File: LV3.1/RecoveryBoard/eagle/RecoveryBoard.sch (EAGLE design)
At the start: 90 parts, among them IC1 BD62120AEFJ-E2, Q6 MOSFET-PCH-SOT23-6, U1 STM32F042K6, U10 TPS63070, Y1 ECS-160-10-36Q-ES-TR

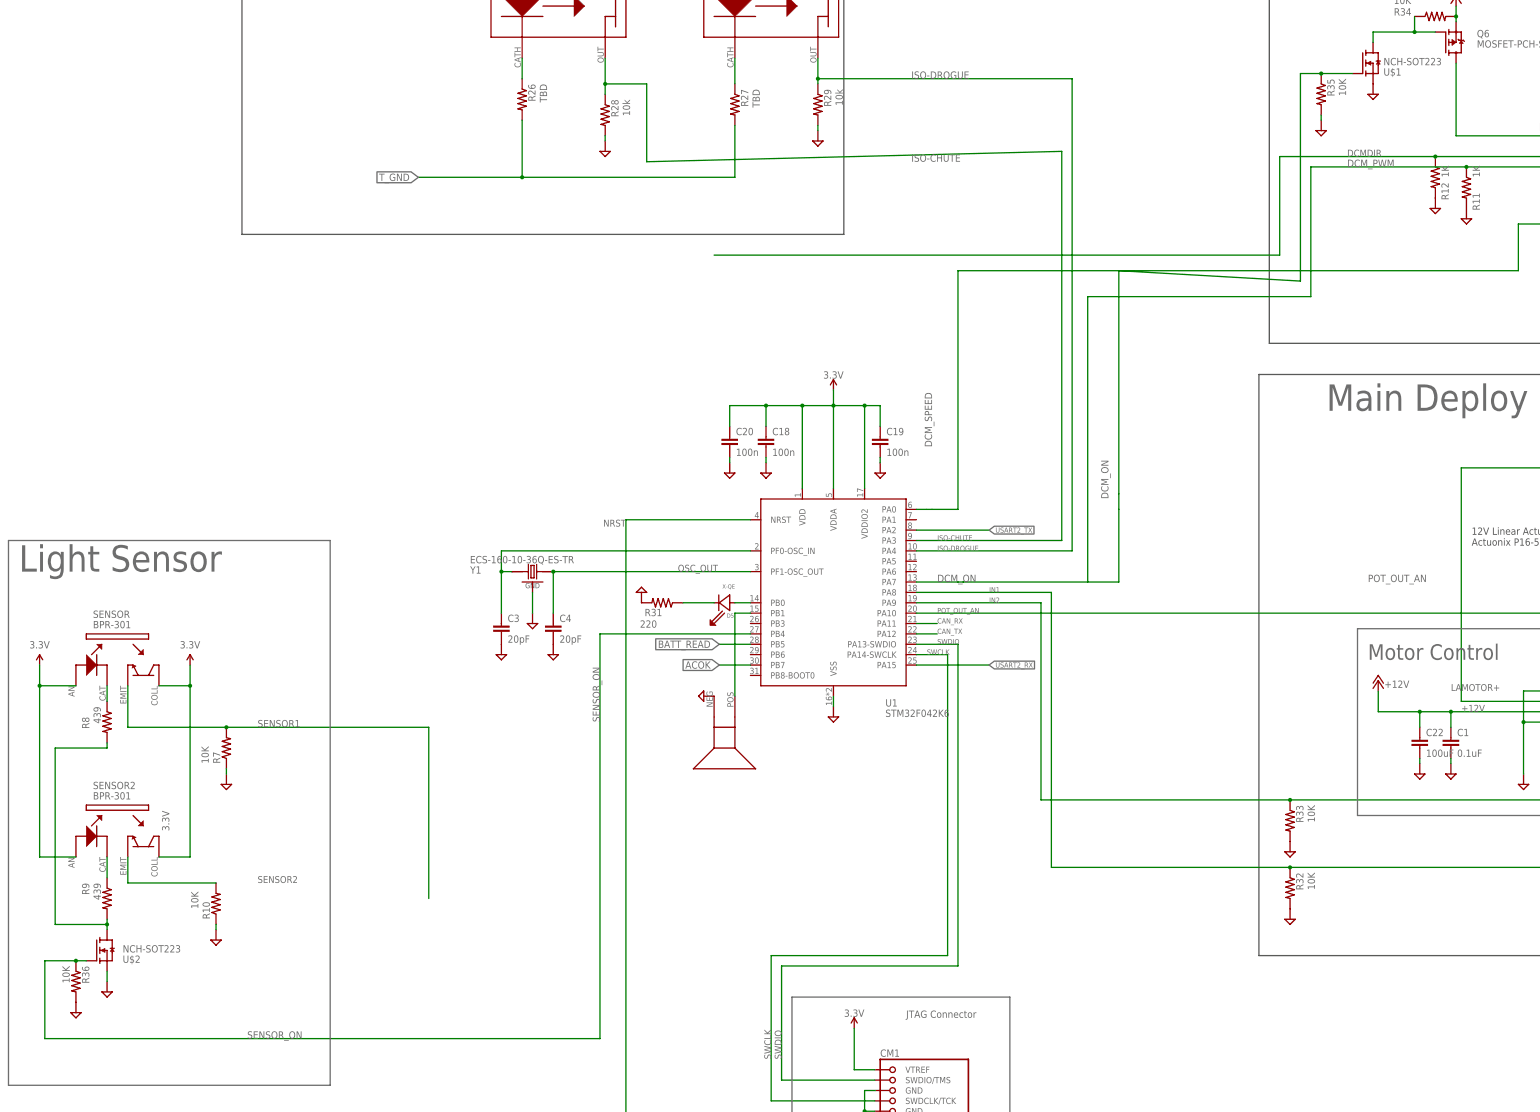
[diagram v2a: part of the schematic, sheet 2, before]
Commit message: beginning routing and placement
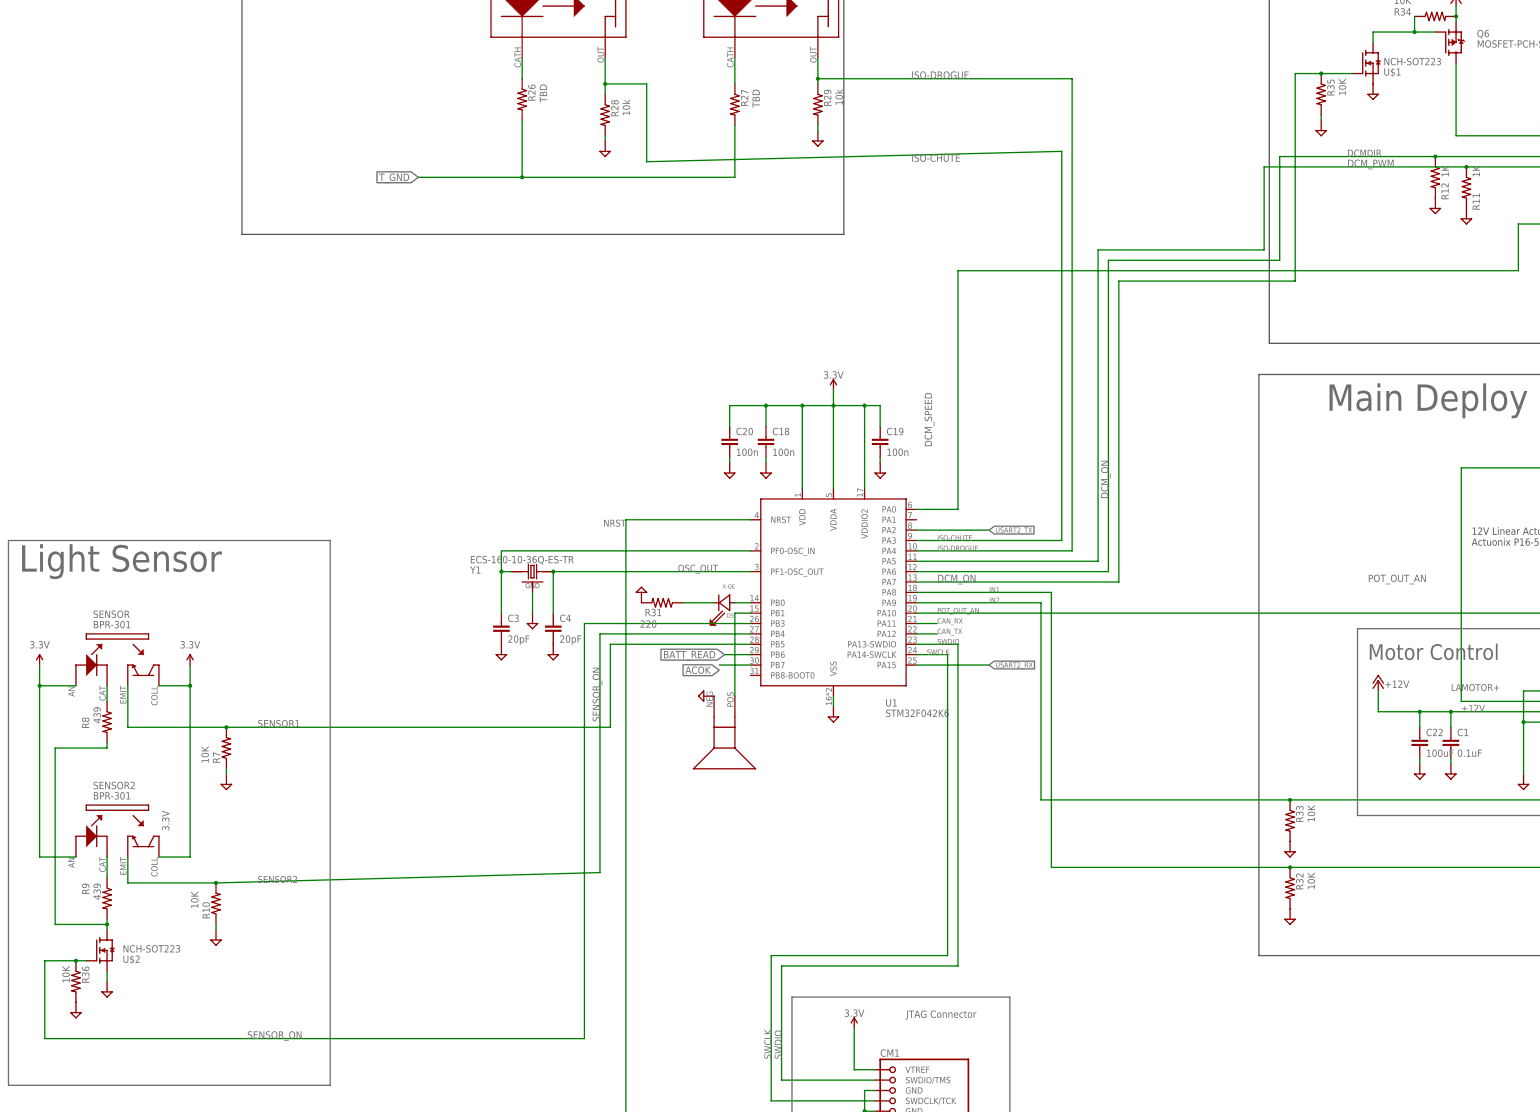
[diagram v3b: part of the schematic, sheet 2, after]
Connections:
- net BATT_READ: now also U1.PB6; no longer U1.PB5
- net DCMDIR: now also U1.PA6
- net DCM_PWM: now also U1.PA5
- net SENSOR1: now also U1.PB5
- net SENSOR2: now also U1.PB4
- net SENSOR_ON: now also U1.PB3; no longer U1.PB4
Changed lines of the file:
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@@
 <net name="SENSOR1" class="0">
 <segment>
-<wire x1="125.73" y1="152.4" x2="175.26" y2="152.4" width="0.1524" layer="91"/>
-<wire x1="175.26" y1="152.4" x2="175.26" y2="110.49" width="0.1524" layer="91"/>
+<wire x1="125.73" y1="152.4" x2="219.71" y2="152.4" width="0.1524" layer="91"/>
 <pinref part="R7" gate="R" pin="2"/>
 <pinref part="SENSOR" gate="BPR-301" pin="EMIT"/>
@@
 <junction x="125.73" y="152.4"/>
 <label x="133.35" y="152.4" size="1.778" layer="95"/>
+<pinref part="U1" gate="G$1" pin="PB5"/>
+<wire x1="219.71" y1="172.72" x2="219.71" y2="152.4" width="0.1524" layer="91"/>
+<wire x1="219.71" y1="172.72" x2="254" y2="172.72" width="0.1524" layer="91"/>
 </segment>
 </net>
@@
 <segment>
 <label x="400.05" y="292.1" size="1.6764" layer="95"/>
-<wire x1="245.11" y1="267.97" x2="383.54" y2="267.97" width="0.1524" layer="91"/>
-<wire x1="383.54" y1="267.97" x2="383.54" y2="292.1" width="0.1524" layer="91"/>
+<wire x1="341.63" y1="266.7" x2="383.54" y2="266.7" width="0.1524" layer="91"/>
+<wire x1="383.54" y1="266.7" x2="383.54" y2="292.1" width="0.1524" layer="91"/>
 <pinref part="J1" gate="A" pin="3"/>
 <wire x1="468.63" y1="292.1" x2="421.64" y2="292.1" width="0.1524" layer="91"/>
@@
 <pinref part="R12" gate="R" pin="1"/>
 <junction x="421.64" y="292.1"/>
+<wire x1="341.63" y1="190.5" x2="341.63" y2="266.7" width="0.1524" layer="91"/>
+<pinref part="U1" gate="G$1" pin="PA6"/>
+<wire x1="294.64" y1="190.5" x2="341.63" y2="190.5" width="0.1524" layer="91"/>
 </segment>
 </net>
 <net name="SENSOR_ON" class="0">
 <segment>
-<wire x1="217.17" y1="175.26" x2="217.17" y2="76.2" width="0.1524" layer="91"/>
-<wire x1="217.17" y1="76.2" x2="81.28" y2="76.2" width="0.1524" layer="91"/>
+<wire x1="213.36" y1="177.8" x2="213.36" y2="76.2" width="0.1524" layer="91"/>
+<wire x1="213.36" y1="76.2" x2="81.28" y2="76.2" width="0.1524" layer="91"/>
 <wire x1="81.28" y1="76.2" x2="81.28" y2="95.25" width="0.1524" layer="91"/>
 <wire x1="81.28" y1="95.25" x2="88.9" y2="95.25" width="0.1524" layer="91"/>
@@
 <wire x1="88.9" y1="95.25" x2="91.44" y2="95.25" width="0.1524" layer="91"/>
 <junction x="88.9" y="95.25"/>
-<pinref part="U1" gate="G$1" pin="PB4"/>
-<wire x1="254" y1="175.26" x2="217.17" y2="175.26" width="0.1524" layer="91"/>
 <label x="217.17" y="153.67" size="1.778" layer="95" rot="R90"/>
 <label x="130.81" y="76.2" size="1.778" layer="95"/>
+<pinref part="U1" gate="G$1" pin="PB3"/>
+<wire x1="213.36" y1="177.8" x2="254" y2="177.8" width="0.1524" layer="91"/>
 </segment>
 </net>
@@
 <wire x1="101.6" y1="114.3" x2="101.6" y2="120.65" width="0.1524" layer="91"/>
 <label x="133.35" y="114.3" size="1.6764" layer="95"/>
+<wire x1="123.19" y1="114.3" x2="217.17" y2="116.84" width="0.1524" layer="91"/>
+<wire x1="217.17" y1="116.84" x2="217.17" y2="175.26" width="0.1524" layer="91"/>
+<junction x="123.19" y="114.3"/>
+<pinref part="U1" gate="G$1" pin="PB4"/>
+<wire x1="254" y1="175.26" x2="217.17" y2="175.26" width="0.1524" layer="91"/>
 </segment>
 </net>
@@
 <pinref part="J1" gate="A" pin="4"/>
 <wire x1="468.63" y1="289.56" x2="429.26" y2="289.56" width="0.1524" layer="91"/>
-<wire x1="429.26" y1="289.56" x2="391.16" y2="289.56" width="0.1524" layer="91"/>
+<wire x1="429.26" y1="289.56" x2="379.73" y2="289.56" width="0.1524" layer="91"/>
 <label x="400.05" y="289.56" size="1.778" layer="95"/>
 <pinref part="R11" gate="R" pin="1"/>
 <junction x="429.26" y="289.56"/>
-<wire x1="391.16" y1="257.81" x2="391.16" y2="289.56" width="0.1524" layer="91"/>
-<wire x1="391.16" y1="257.81" x2="336.55" y2="257.81" width="0.1524" layer="91"/>
-<wire x1="336.55" y1="257.81" x2="336.55" y2="187.96" width="0.1524" layer="91"/>
+<wire x1="379.73" y1="269.24" x2="379.73" y2="289.56" width="0.1524" layer="91"/>
+<wire x1="379.73" y1="269.24" x2="339.09" y2="269.24" width="0.1524" layer="91"/>
+<pinref part="U1" gate="G$1" pin="PA5"/>
+<wire x1="339.09" y1="193.04" x2="339.09" y2="269.24" width="0.1524" layer="91"/>
+<wire x1="339.09" y1="193.04" x2="294.64" y2="193.04" width="0.1524" layer="91"/>
 </segment>
 </net>
@@
 <pinref part="R35" gate="R" pin="1"/>
 <wire x1="401.32" y1="312.42" x2="393.7" y2="312.42" width="0.1524" layer="91"/>
-<wire x1="393.7" y1="312.42" x2="388.62" y2="312.42" width="0.1524" layer="91"/>
-<wire x1="388.62" y1="312.42" x2="388.62" y2="261.62" width="0.1524" layer="91"/>
-<wire x1="388.62" y1="261.62" x2="344.17" y2="264.16" width="0.1524" layer="91"/>
+<wire x1="393.7" y1="312.42" x2="387.35" y2="312.42" width="0.1524" layer="91"/>
+<wire x1="387.35" y1="312.42" x2="387.35" y2="261.62" width="0.1524" layer="91"/>
+<wire x1="387.35" y1="261.62" x2="344.17" y2="261.62" width="0.1524" layer="91"/>
 <junction x="393.7" y="312.42"/>
 <label x="341.63" y="208.28" size="1.778" layer="95" rot="R90"/>
-<wire x1="344.17" y1="264.16" x2="344.17" y2="209.55" width="0.1524" layer="91"/>
+<wire x1="344.17" y1="261.62" x2="344.17" y2="187.96" width="0.1524" layer="91"/>
 <pinref part="U1" gate="G$1" pin="PA7"/>
-<wire x1="344.17" y1="209.55" x2="344.17" y2="205.74" width="0.1524" layer="91"/>
-<wire x1="306.07" y1="187.96" x2="304.8" y2="187.96" width="0.1524" layer="91"/>
 <label x="299.72" y="187.96" size="1.778" layer="95"/>
-<wire x1="304.8" y1="187.96" x2="294.64" y2="187.96" width="0.1524" layer="91"/>
-<wire x1="306.07" y1="187.96" x2="344.17" y2="187.96" width="0.1524" layer="91"/>
-<wire x1="344.17" y1="187.96" x2="344.17" y2="205.74" width="0.1524" layer="91"/>
+<wire x1="294.64" y1="187.96" x2="344.17" y2="187.96" width="0.1524" layer="91"/>
 </segment>
 </net>
@@
 </segment>
 </net>
-<net name="BATT_READ" class="0">
-<segment>
-<pinref part="U1" gate="G$1" pin="PB5"/>
-<wire x1="254" y1="172.72" x2="246.38" y2="172.72" width="0.1524" layer="91"/>
-<label x="246.38" y="172.72" size="1.778" layer="95" rot="R180" xref="yes"/>
-</segment>
-</net>
 <net name="CAN_RX" class="0">
 <segment>
@@
 <pinref part="U1" gate="G$1" pin="PB7"/>
 <wire x1="254" y1="167.64" x2="246.38" y2="167.64" width="0.1524" layer="91"/>
-<label x="246.38" y="167.64" size="1.778" layer="95" rot="R180" xref="yes"/>
+<label x="246.38" y="166.37" size="1.778" layer="95" rot="R180" xref="yes"/>
 </segment>
 </net>
@@
 </segment>
 </net>
+<net name="BATT_READ" class="0">
+<segment>
+<pinref part="U1" gate="G$1" pin="PB6"/>
+<wire x1="254" y1="170.18" x2="247.65" y2="170.18" width="0.1524" layer="91"/>
+<label x="247.65" y="170.18" size="1.778" layer="95" rot="R180" xref="yes"/>
+</segment>
+</net>

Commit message: finished routing
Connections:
- net N$3 renamed OSC_IN
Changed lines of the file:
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@@
 <?xml version="1.0" encoding="utf-8"?>
 <!DOCTYPE eagle SYSTEM "eagle.dtd">
-<eagle version="9.5.1">
+<eagle version="9.4.2">
 <drawing>
 <settings>
@@
 </segment>
 </net>
-<net name="N$3" class="0">
-<segment>
-<pinref part="U1" gate="G$1" pin="PF0-OSC_IN"/>
-<wire x1="254" y1="195.58" x2="193.04" y2="195.58" width="0.1524" layer="91"/>
+<net name="OSC_IN" class="0">
+<segment>
 <pinref part="Y1" gate="G$1" pin="IN/OUT"/>
 <pinref part="C3" gate="CE" pin="1"/>
@@
 <wire x1="193.04" y1="195.58" x2="193.04" y2="190.5" width="0.1524" layer="91"/>
 <junction x="193.04" y="190.5"/>
-</segment>
-</net>
+<pinref part="U1" gate="G$1" pin="PF0-OSC_IN"/>
+<wire x1="193.04" y1="195.58" x2="254" y2="195.58" width="0.1524" layer="91"/>
+<label x="237.49" y="195.58" size="1.778" layer="95"/>
+</segment>
+</net>
